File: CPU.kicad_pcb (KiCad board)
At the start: 2 copper layers, 157 x 85.3 mm, 91 parts, among them J101 Conn_02x10_Odd_Even, J102 Conn_02x14_Odd_Even_MountingP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, J201 1X4SMD-FPC, J301 Conn_02x03_Odd_Even, Q101 IRLML0040TR, Q102 IRLML0040TR, Q103 DMC4050, Q301 IRLML0040TR, Q302 IRLML0040TR, SW101 SW_SPDT, SW301 TACTILE_SWITCHPTS540-SMD, SW302 TACTILE_SWITCHPTS540-SMD, SW303 TACTILE_SWITCHPTS540-SMD, SW304 TACTILE_SWITCHPTS540-SMD, SW305 TACTILE_SWITCHPTS540-SMD, SW306 TACTILE_SWITCHPTS540-SMD, SW307 TACTILE_SWITCHPTS540-SMD, SW308 TACTILE_SWITCHPTS540-SMD, SW309 TACTILE_SWITCHPTS540-SMD, SW310 TACTILE_SWITCHPTS540-SMD, SW311 TACTILE_SWITCHPTS540-SMD, SW312 TACTILE_SWITCHPTS540-SMD, SW313 TACTILE_SWITCHPTS540-SMD, U101 ATtiny85-20PU, U201 OPT3001, U202 AT42QT1070-SSUR, U301 ATMEGA328P_TQFP, Y301 Resonator_Small

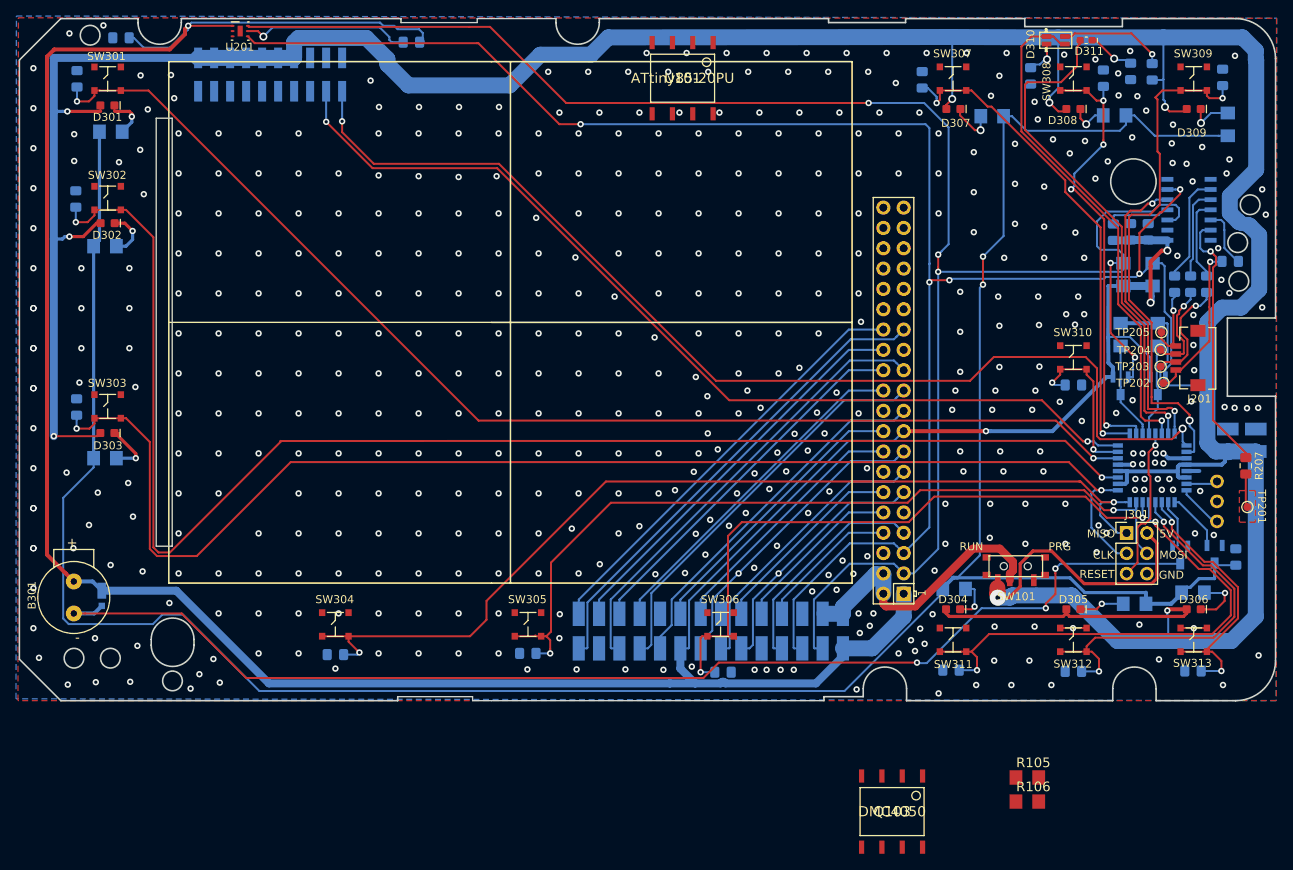
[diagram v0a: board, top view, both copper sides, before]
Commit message: Last version before switching to resistive model to read the scroll wheel.
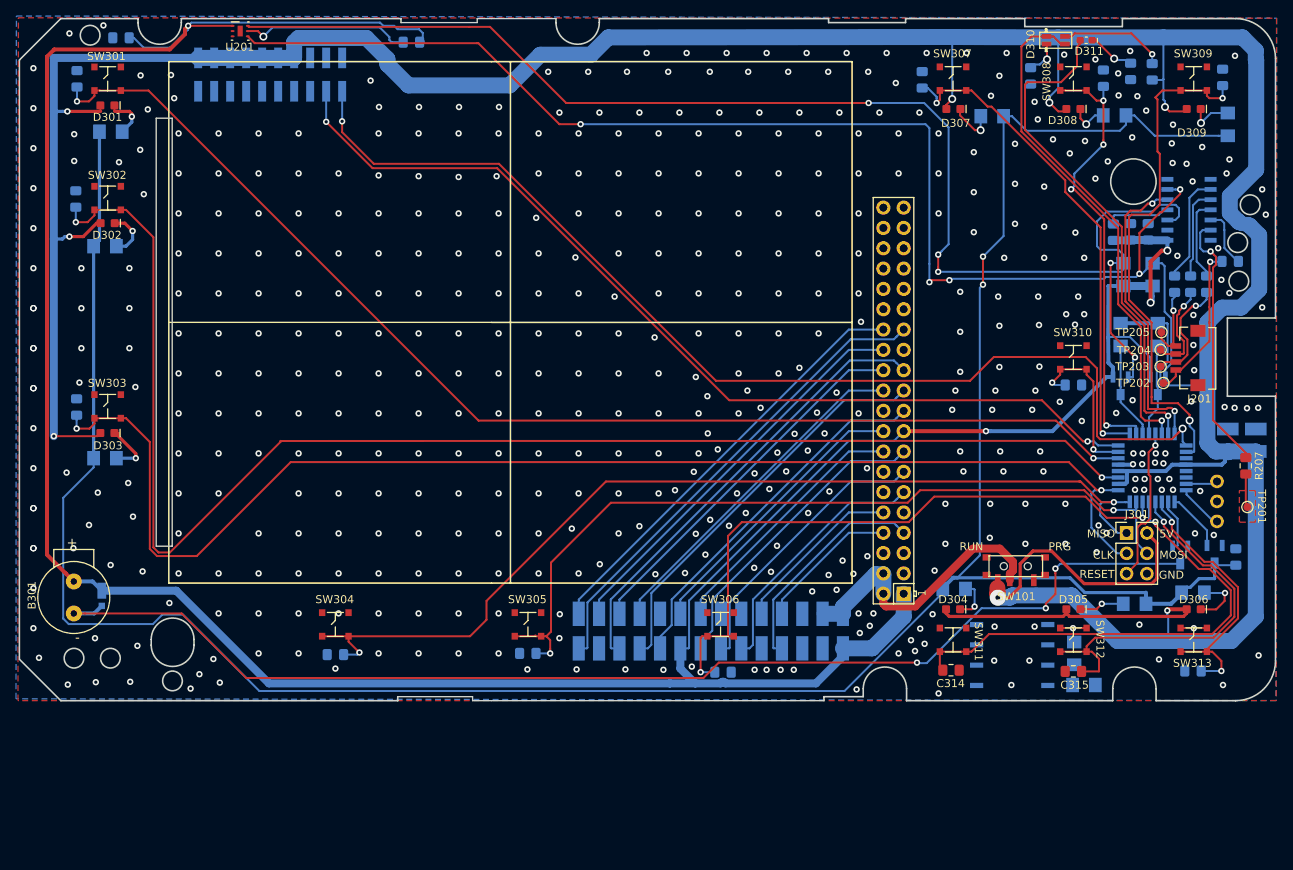
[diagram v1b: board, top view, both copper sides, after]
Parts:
- removed Q103: DMC4050, Marco:8-SMD
- removed R105, R106: 10K, CPU:R1206
- removed U101: ATtiny85-20PU, Marco:8-SMD
- added Q201: DMC4050, Marco:8-SMD, B.Cu at (154.5, 125.1)
- added R208: 10K, CPU:R1206, B.Cu at (162.2, 124.9)
- added R209: 10K, CPU:R1206, B.Cu at (163.5, 128.8)
- C314, C315: moved to F.Cu
- U301: value ATMEGA328P_TQFP -> ATmega328PB-AU; footprint CPU:TQFP32-08 -> Package_QFP:TQFP-32_7x7mm_P0.8mm
- turned C314 to 180 degrees
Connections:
- J102 pad 3: /SDA -> Net-(J102-Pad3)
- J102 pad 5: /SCL -> Net-(J102-Pad5)
- Pi101 pad 12: /Pi12 -> /SDA
- Pi101 pad 3: /SDA -> Net-(Pi101-Pad3)
- Pi101 pad 35: Net-(Pi101-Pad35) -> /SCL
- Pi101 pad 5: /SCL -> Net-(Pi101-Pad5)
- SW101 pad 3: 5V -> +5VP
- U301 pad 3: GND -> /Micro Controller Devices/PI_PWR_SW
- U301 pad 6: 5V -> /Micro Controller Devices/PI_RESET_TOGGLE
- Y301 pad 1: Net-(U301-Pad8) -> Net-(U301-Pad7)
- Y301 pad 3: Net-(U301-Pad7) -> Net-(U301-Pad8)
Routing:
- net /SDA: track 235.8 -> 174.8 mm
- net /SCL: track 228.9 -> 169.3 mm
- net /Pi12: track 25.1 -> 0.00 mm
- net GND: track 13.3 -> 8.57 mm, vias 487 -> 486
- net /Micro Controller Devices/SWW: track 62.6 -> 60.2 mm, vias 2 -> 1
- net 5V: track 490.7 -> 489.5 mm
- net /Pi15: vias 1 -> 0
- net /Pi11: vias 1 -> 0
- net /Micro Controller Devices/SWP: vias 2 -> 1

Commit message: Version 2, DRC and ERC clear, ready to send, waiting on V1 to see what did not work.
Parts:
- removed R202, R203, R204, R205, R206, R207: 10K, Resistor_SMD:R_0805_2012Metric_Pad1.15x1.40mm_HandSolder
- added C101: 47uF, Capacitor_SMD:C_0805_2012Metric_Pad1.15x1.40mm_HandSolder, F.Cu at (184.0, 101.0)
- added J303: Conn_02x03_Odd_Even, Connector_PinHeader_2.54mm:PinHeader_2x03_P2.54mm_Vertical, F.Cu at (179.5, 60.0)
- added TP101: PI_RESET, TestPoint:TestPoint_Pad_D1.0mm, F.Cu at (139.5, 64.0)
- SW101: moved to B.Cu
- U202: value AT42QT1070-SSUR -> ATTINY84ATTINY84-20PU; footprint UltraLibrarian:AT42QT1070-SSUR -> MarcoK:14SOIC
- moved C204 51.7 mm to (155.0, 69.0), turned to 270 degrees
- moved Q301 48.0 mm to (158.5, 69.5), turned to 180 degrees
- moved R209 10.8 mm to (160.5, 118.5), turned to 270 degrees
- moved Y301 4.92 mm to (180.5, 103.5), turned to 270 degrees
- moved R208 2.03 mm to (161.0, 126.5), turned to 270 degrees
- moved Q201 1.50 mm to (153.0, 125.0)
- moved R309 1.05 mm to (182.5, 58.8)
- moved C202 1.00 mm to (170.5, 72.2)
- moved C203 0.80 mm to (168.5, 72.2)
- moved SW101 0.55 mm to (155.5, 114.0)
- moved TP304 0.41 mm to (173.0, 91.0)
- moved C315 0.38 mm to (162.5, 127.0), turned to 180 degrees
- moved TP301 0.29 mm to (173.0, 85.0)
- moved TP302 0.07 mm to (173.0, 87.0)
- moved TP303 0.07 mm to (173.0, 89.0)
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- renumbered C302 to C204, J201 to J302, TP201 to TP102, TP205 to TP301, TP204 to TP302, TP203 to TP303, TP202 to TP304
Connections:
- net /Micro Controller Devices/PI_RESET_TOGGLE renamed Net-(U301-Pad6)
- D310 pad 1: /Micro Controller Devices/R_G -> /I2C Devices/R_G
- D310 pad 4: /Micro Controller Devices/R_G -> /I2C Devices/R_G
- D311 pad A: /Micro Controller Devices/ORANGE -> /I2C Devices/ORANGE
- J302 pad 1: /I2C Devices/ED -> /I2C Devices/SCC
- J302 pad 2: /I2C Devices/EC -> /I2C Devices/SCR3
- J302 pad 3: /I2C Devices/EB -> /I2C Devices/SCR2
- J302 pad 4: /I2C Devices/EA -> /I2C Devices/SCR1
- Q301 pad 1: /Micro Controller Devices/LED_PWM -> /I2C Devices/LED_PWM
- TP102 pad 1: /I2C Devices/TGUARD -> /TGUARD
- TP301 pad 1: /I2C Devices/ED -> /I2C Devices/SCC
- TP302 pad 1: /I2C Devices/EC -> /I2C Devices/SCR3
- TP303 pad 1: /I2C Devices/EB -> /I2C Devices/SCR2
- TP304 pad 1: /I2C Devices/EA -> /I2C Devices/SCR1
- U202 pad 10: Net-(R204-Pad1) -> /I2C Devices/SCC
- U202 pad 11: Net-(R205-Pad1) -> /I2C Devices/SCR3
- U202 pad 12: Net-(R206-Pad1) -> /I2C Devices/SCR2
- U202 pad 13: Net-(R207-Pad1) -> /I2C Devices/SCR1
- U202 pad 2: GND -> Net-(U202-Pad2)
- U202 pad 3: /SDA -> /I2C Devices/R_G
- U202 pad 4: Net-(R202-Pad1) -> /I2C Devices/85RES
- U202 pad 5: /I2C Devices/TINT -> /I2C Devices/SCROLL_INT
- U202 pad 6: /SCL -> /I2C Devices/ORANGE
- U202 pad 7: Net-(U202-Pad7) -> /SDA
- U202 pad 8: Net-(U202-Pad8) -> /I2C Devices/LED_PWM
- U202 pad 9: Net-(R203-Pad1) -> /SCL
- U301 pad 3: /Micro Controller Devices/PI_PWR_SW -> Net-(U301-Pad3)
- U301 pad 30: /Micro Controller Devices/R_G -> /PI_RESET_TOGGLE
- U301 pad 31: /Micro Controller Devices/ORANGE -> /I2C Devices/SCROLL_INT
- U301 pad 32: /I2C Devices/TINT -> /I2C Devices/85RES
- U301 pad 9: /Micro Controller Devices/LED_PWM -> /Micro Controller Devices/PI_PWR_SW
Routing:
- net /PI_RESET_TOGGLE: track 0.00 -> 66.3 mm, vias 0 -> 5
- net /Micro Controller Devices/PI_PWR_SW: track 0.00 -> 63.8 mm, vias 0 -> 2
- net /Micro Controller Devices/R_G: track 63.5 -> 0.00 mm, vias 1 -> 0
- net /Micro Controller Devices/ORANGE: track 63.3 -> 0.00 mm, vias 1 -> 0
- net /I2C Devices/ORANGE: track 0.00 -> 42.3 mm, vias 0 -> 1
- net /I2C Devices/R_G: track 0.00 -> 41.7 mm, vias 0 -> 1
- net /I2C Devices/85RES: track 0.00 -> 41.3 mm, vias 0 -> 5
- net /I2C Devices/TINT: track 37.8 -> 0.00 mm, vias 2 -> 0
- net /I2C Devices/SCROLL_INT: track 0.00 -> 36.9 mm, vias 0 -> 2
- net /SDA: track 174.8 -> 211.1 mm, vias 5 -> 7
- net /I2C Devices/LED_PWM: track 0.00 -> 35.8 mm
- net Net-(R207-Pad1): track 32.8 -> 0.00 mm, vias 1 -> 0
- net +5VP: track 0.00 -> 24.5 mm
- net /I2C Devices/SCR2: track 0.00 -> 24.5 mm, vias 0 -> 1
- net /I2C Devices/SCR1: track 0.00 -> 24.3 mm, vias 0 -> 1
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- added copper zone on F.Cu, net /TGUARD
- removed copper zone on F.Cu, net /I2C Devices/TGUARD
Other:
- board text added: "CR101 CPU Board V2 mquezada 20200423"
